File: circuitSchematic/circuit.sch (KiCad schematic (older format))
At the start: 5 parts, among them M1 Motor_DC, Q1 Q_NPN_BCEC

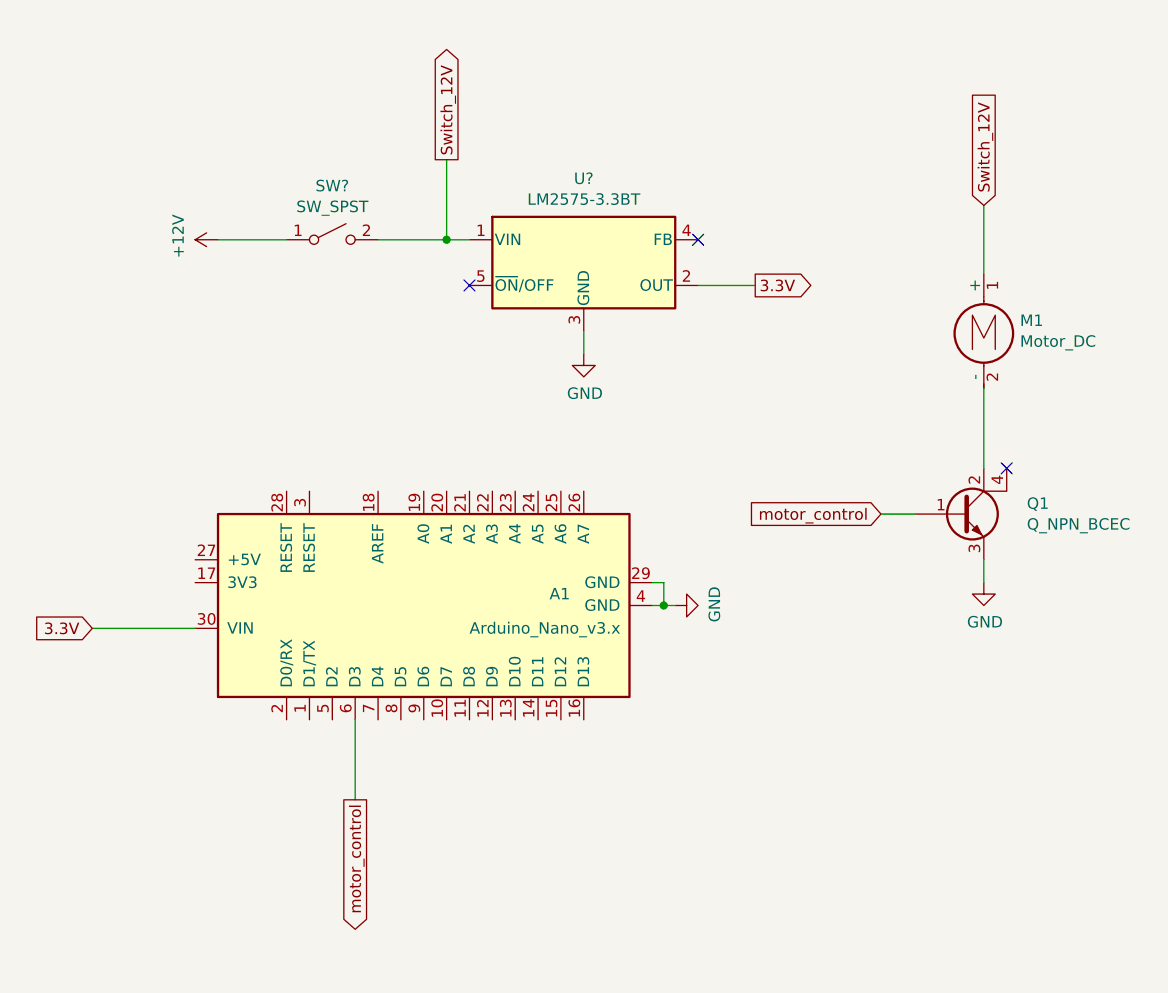
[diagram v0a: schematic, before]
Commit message: Updated Vin voltage value, from 3.3V to 5V
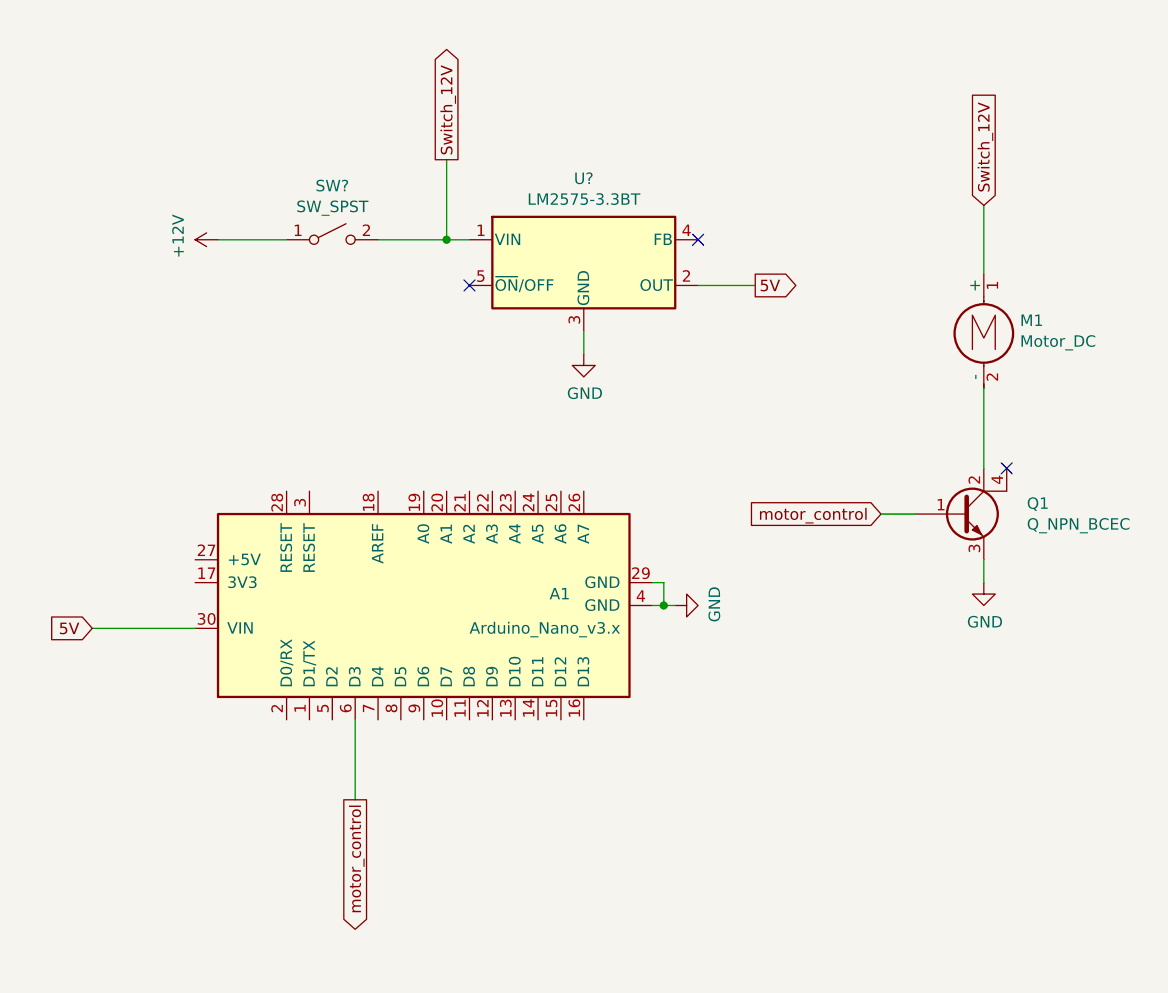
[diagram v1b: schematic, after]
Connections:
- net 3.3V renamed 5V
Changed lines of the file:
@@
 EESchema Schematic File Version 4
-LIBS:test-cache
+LIBS:circuit-cache
 EELAYER 26 0
 EELAYER END
@@
 NoConn ~ 2900 2000
 Text GLabel 4150 2000 2    50   Output ~ 0
-3.3V
+5V
 Wire Wire Line
 	3900 2000 4150 2000
-Text GLabel 1250 3500 0    50   Input ~ 0
-3.3V
 Wire Wire Line
 	1250 3500 1700 3500
@@
 Wire Wire Line
 	2800 1800 2900 1800
+Text GLabel 1250 3500 0    50   Input ~ 0
+5V
 $EndSCHEMATC

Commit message: Fixed output pin from D3 to D7 and added indicator LED to pin D6
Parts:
- added D?: LED, symbol Device:LED
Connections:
- net labels added: 3.3V
- net labels removed: 5V
- wire segments 16 -> 19
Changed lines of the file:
@@
 Wire Wire Line
 	5150 2450 5150 2800
-Text GLabel 2400 4250 3    50   Output ~ 0
-motor_control
-Wire Wire Line
-	2400 3900 2400 4250
 $Comp
 L Regulator_Switching:LM2575-3.3BT U?
@@
 NoConn ~ 2900 2000
 Text GLabel 4150 2000 2    50   Output ~ 0
-5V
+3.3V
 Wire Wire Line
 	3900 2000 4150 2000
+Text GLabel 1250 3500 0    50   Input ~ 0
+3.3V
 Wire Wire Line
 	1250 3500 1700 3500
@@
 Wire Wire Line
 	2800 1800 2900 1800
-Text GLabel 1250 3500 0    50   Input ~ 0
-5V
+Text GLabel 2800 4250 3    50   Output ~ 0
+motor_control
+Wire Wire Line
+	2800 3900 2800 4250
+$Comp
+L Device:LED D?
+U 1 1 5C79E6C3
+P 2600 4300
+F 0 "D?" V 2638 4183 50  0000 R CNN
+F 1 "LED" V 2547 4183 50  0000 R CNN
+F 2 "" H 2600 4300 50  0001 C CNN
+F 3 "~" H 2600 4300 50  0001 C CNN
+	1    2600 4300
+	0    -1   -1   0
+$EndComp
+Wire Wire Line
+	2700 3900 2700 4150
+Wire Wire Line
+	2700 4150 2600 4150
+$Comp
+L power:GND #PWR?
+U 1 1 5C79E931
+P 2600 4600
+F 0 "#PWR?" H 2600 4350 50  0001 C CNN
+F 1 "GND" H 2605 4427 50  0000 C CNN
+F 2 "" H 2600 4600 50  0001 C CNN
+F 3 "" H 2600 4600 50  0001 C CNN
+	1    2600 4600
+	1    0    0    -1
+$EndComp
+Wire Wire Line
+	2600 4450 2600 4600
 $EndSCHEMATC
